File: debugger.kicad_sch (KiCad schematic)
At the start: 15 parts, among them J2 MCU_SWD, J3 TC_SWD, U2 ATSAMD11

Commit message: schematic wip
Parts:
- removed D7: SCHOTTKY, mainboard:DSN1006-2, symbol Device:D_Schottky
- C1, C3: Part Number CL05A105MQ5NNNC -> CL05A105KP5NNNC; Substitution CL05A105KQ5NNNC, CL05A105KP5NNNC, CL05A105KO5NNNC -> any equivalent
- C2: value 2.2uF -> 10uF; Part Number CL10A225KP8NNNC -> CL10A106KP8NNNC
- J2, R1: DNP DNP -> (none); now not fitted
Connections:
- net CONTROL_MCU_D+ renamed MCU_D+
- net CONTROL_MCU_D- renamed MCU_D-
- net CONTROL_RESET_DETECT renamed USB_RESET_DETECT
- net CONTROL_SWITCH renamed USB_SWITCH
- net LED10 renamed LED1
- net LED11 renamed LED2
- net LED12 renamed LED3
- net LED13: no longer names the net of U2.16 (PA23)
- net LED14: no longer names the net of U2.17 (PA27)
- net MCU_SWDCLK renamed MCU_SWCLK
- no-connect marks 2 -> 5
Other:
- note added: "FIXME do something with spare pins? bi-directional MCU/FPGA UART?"
- note added: "VDD: must be 3.3 V for USB operation"
- note removed: "debug LEDs A-E"
- moved on the sheet: C1, R2, R3, TP1, TP2, TP3

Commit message: update symbol metadata
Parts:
- R1: Manufacturer Yageo -> (none); Substitution any equivalent -> (none)
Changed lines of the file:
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@@
       (effects (font (size 1.27 1.27)) hide)
     )
-    (property "Substitution" "any equivalent" (at 198.12 46.99 0)
+    (property "Substitution" "" (at 198.12 46.99 0)
       (effects (font (size 1.27 1.27)) hide)
     )
@@
       (effects (font (size 1.27 1.27)) hide)
     )
-    (property "Manufacturer" "Yageo" (at 198.12 46.99 0)
+    (property "Manufacturer" "" (at 198.12 46.99 0)
       (effects (font (size 1.27 1.27)) hide)
     )

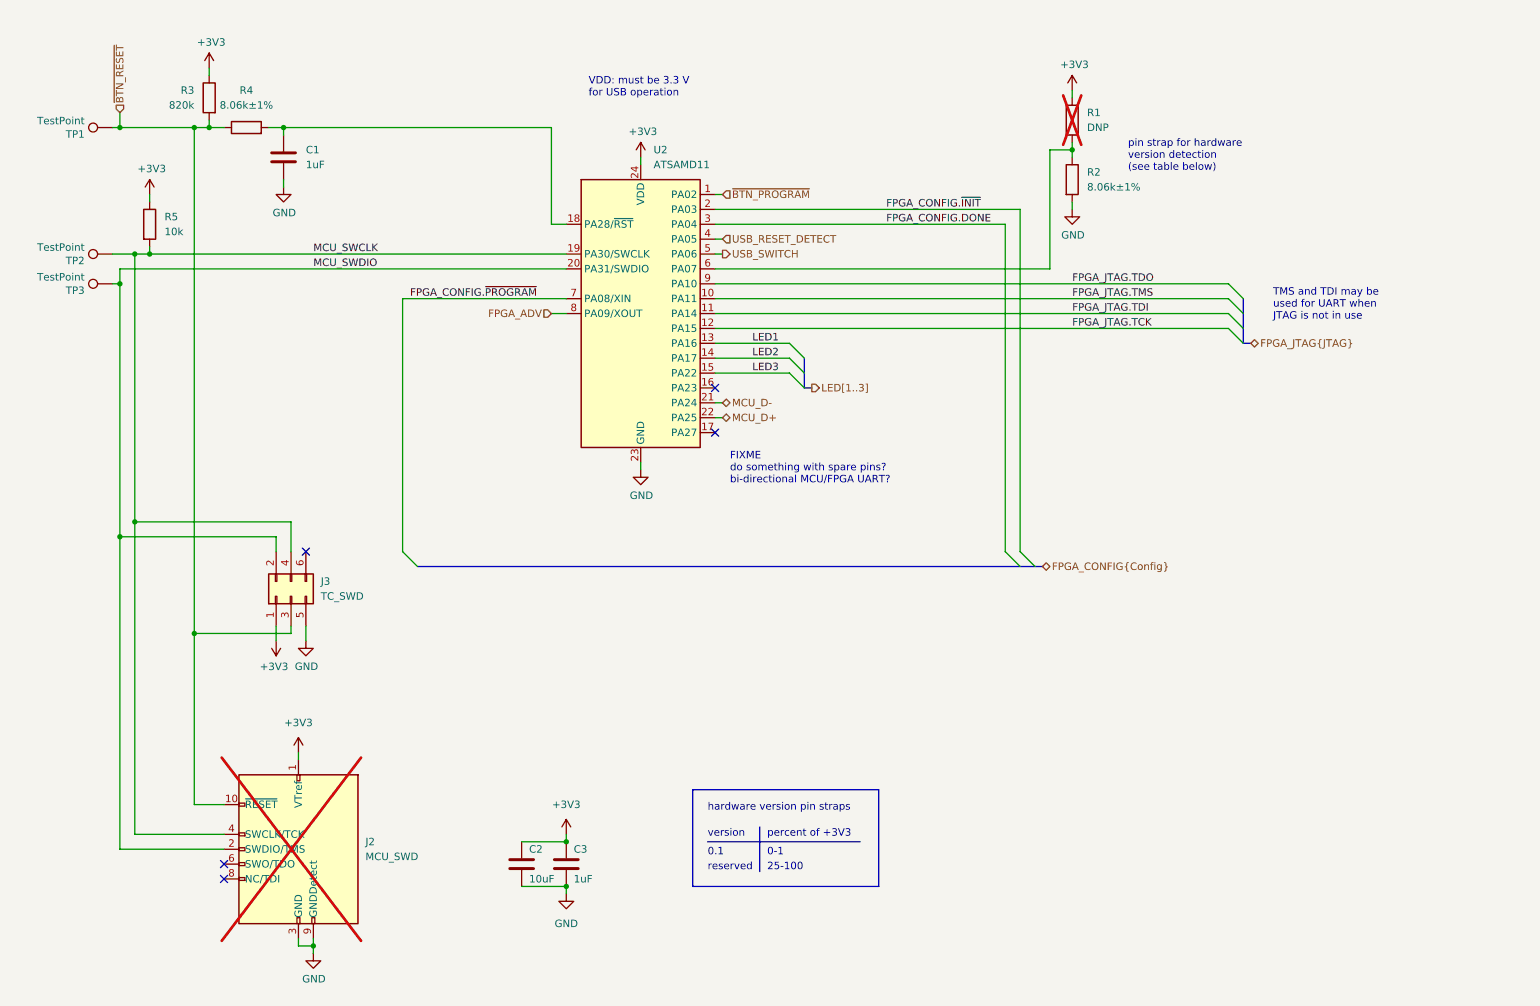
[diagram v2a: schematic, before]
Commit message: complete initial layout
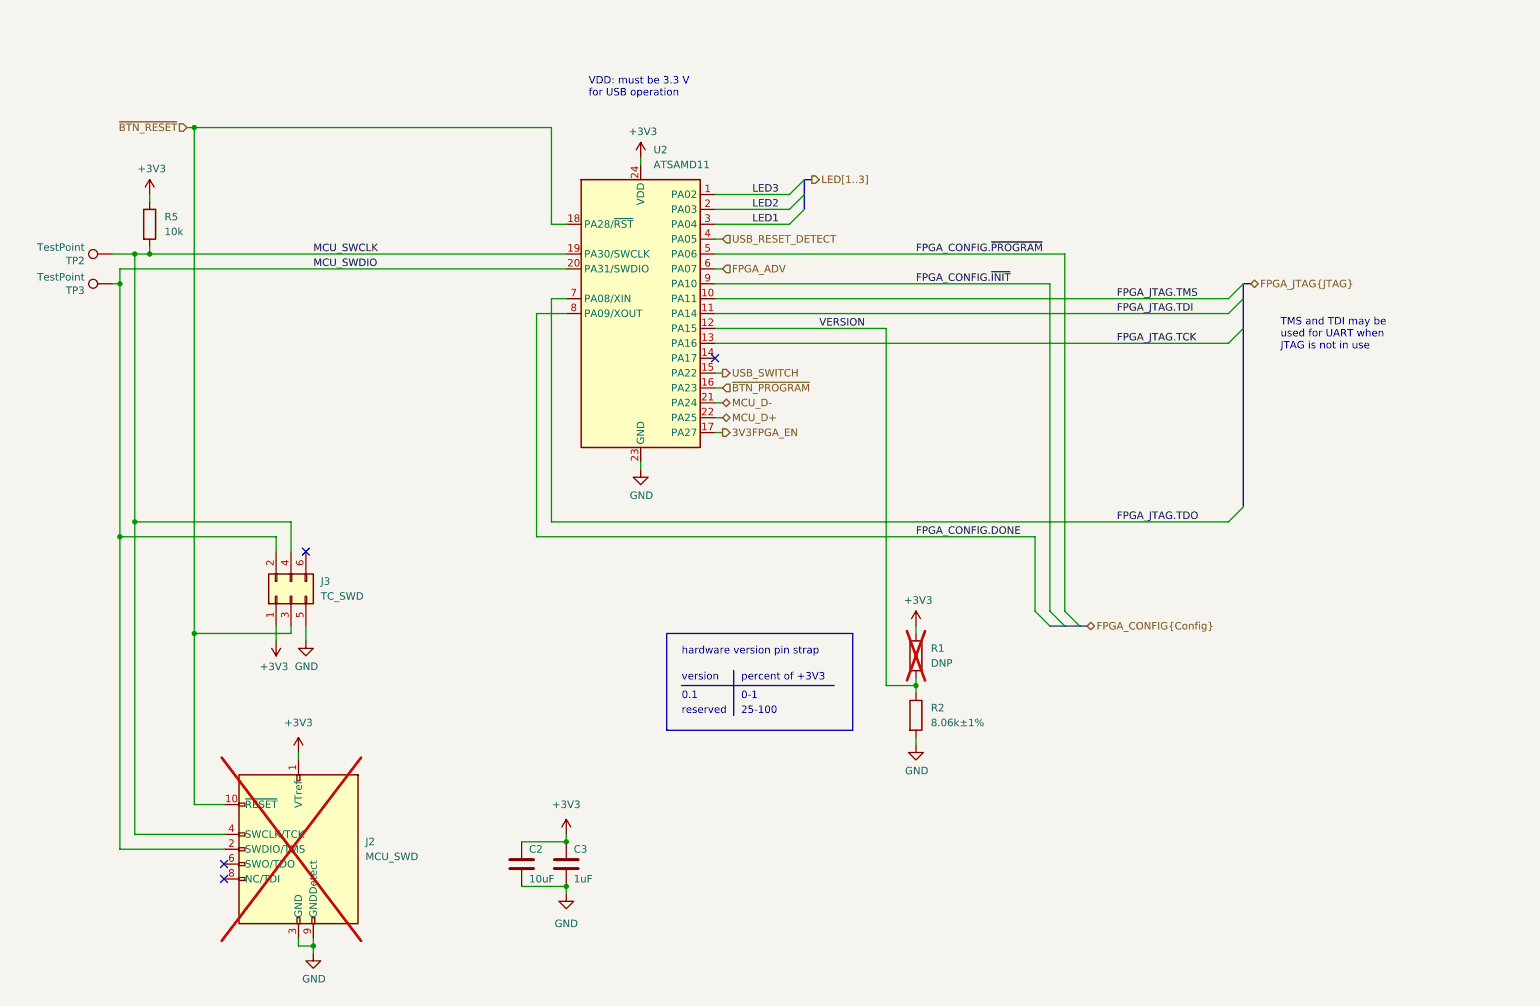
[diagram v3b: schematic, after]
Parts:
- removed C1: 1uF, Capacitor_SMD:C_0402_1005Metric, symbol Device:C
- removed R3: 820k, Resistor_SMD:R_0402_1005Metric, symbol Device:R
- removed R4: 8.06k±1%, Resistor_SMD:R_0402_1005Metric, symbol Device:R
- removed TP1: TestPoint, TestPoint:TestPoint_Pad_D1.0mm, symbol Connector:TestPoint
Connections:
- net FPGA_ADV: now also U2.6 (PA07); no longer U2.8 (PA09/XOUT)
- net FPGA_CONFIG.DONE: now also U2.8 (PA09/XOUT); no longer U2.3 (PA04)
- net FPGA_CONFIG.~{INIT}: now also U2.9 (PA10); no longer U2.2 (PA03)
- net FPGA_CONFIG.~{PROGRAM}: now also U2.5 (PA06); no longer U2.7 (PA08/XIN)
- net FPGA_JTAG.TCK: now also U2.13 (PA16); no longer U2.12 (PA15)
- net FPGA_JTAG.TDO: now also U2.7 (PA08/XIN); no longer U2.9 (PA10)
- net LED1: now also U2.3 (PA04); no longer U2.13 (PA16)
- net LED2: now also U2.2 (PA03); no longer U2.14 (PA17)
- net LED3: now also U2.1 (PA02); no longer U2.15 (PA22)
- net USB_SWITCH: now also U2.15 (PA22); no longer U2.5 (PA06)
- net ~{BTN_PROGRAM}: now also U2.16 (PA23); no longer U2.1 (PA02)
- net ~{BTN_RESET}: now also U2.18 (PA28/~{RST})
- net 3V3FPGA_EN: now reaches U2.17 (PA27)
- net VERSION: now reaches R1.2, R2.1
- net VERSION: now also U2.12 (PA15); no longer U2.6 (PA07)
- no-connect marks 5 -> 4
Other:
- note added: "hardware version pin strap"
- note removed: "FIXME do something with spare pins? bi-directional MCU/FPGA UART?"
- note removed: "hardware version pin straps"
- note removed: "pin strap for hardware version detection (see table below)"
- moved on the sheet: R1, R2

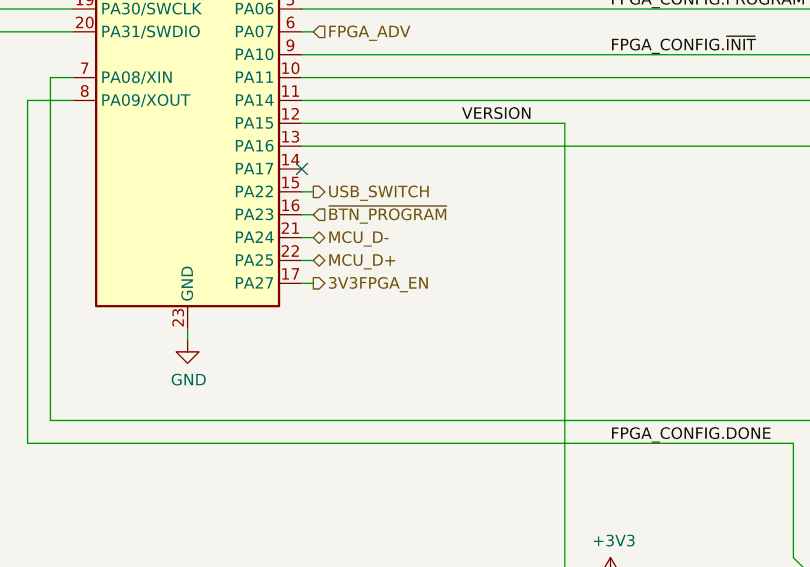
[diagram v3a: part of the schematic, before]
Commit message: invert 3V3FPGA_EN
The mcu has default pull-up, not pull-down.
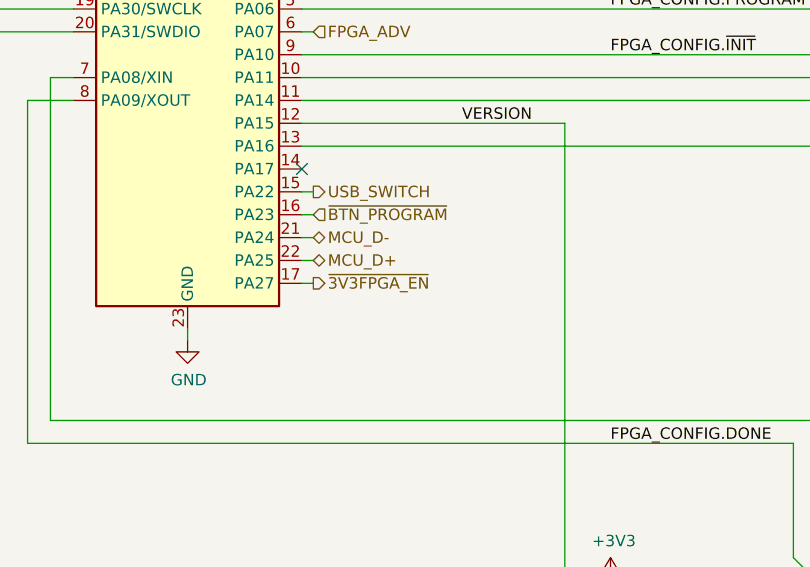
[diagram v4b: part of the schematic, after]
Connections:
- net 3V3FPGA_EN renamed ~{3V3FPGA_EN}
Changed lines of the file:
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@@
     (effects (font (size 1.27 1.27)) (justify left))
   )
-  (hierarchical_label "3V3FPGA_EN" (shape output) (at 138.43 100.33 0) (fields_autoplaced)
+  (hierarchical_label "~{3V3FPGA_EN}" (shape output) (at 138.43 100.33 0) (fields_autoplaced)
     (effects (font (size 1.27 1.27)) (justify left))
   )
